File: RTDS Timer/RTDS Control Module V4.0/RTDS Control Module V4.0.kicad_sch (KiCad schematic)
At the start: 13 parts, among them J1 PH1-10-UA, K1 G6L-1P_DC5, U1 NE555D, U2 IRLML2060TRPBF

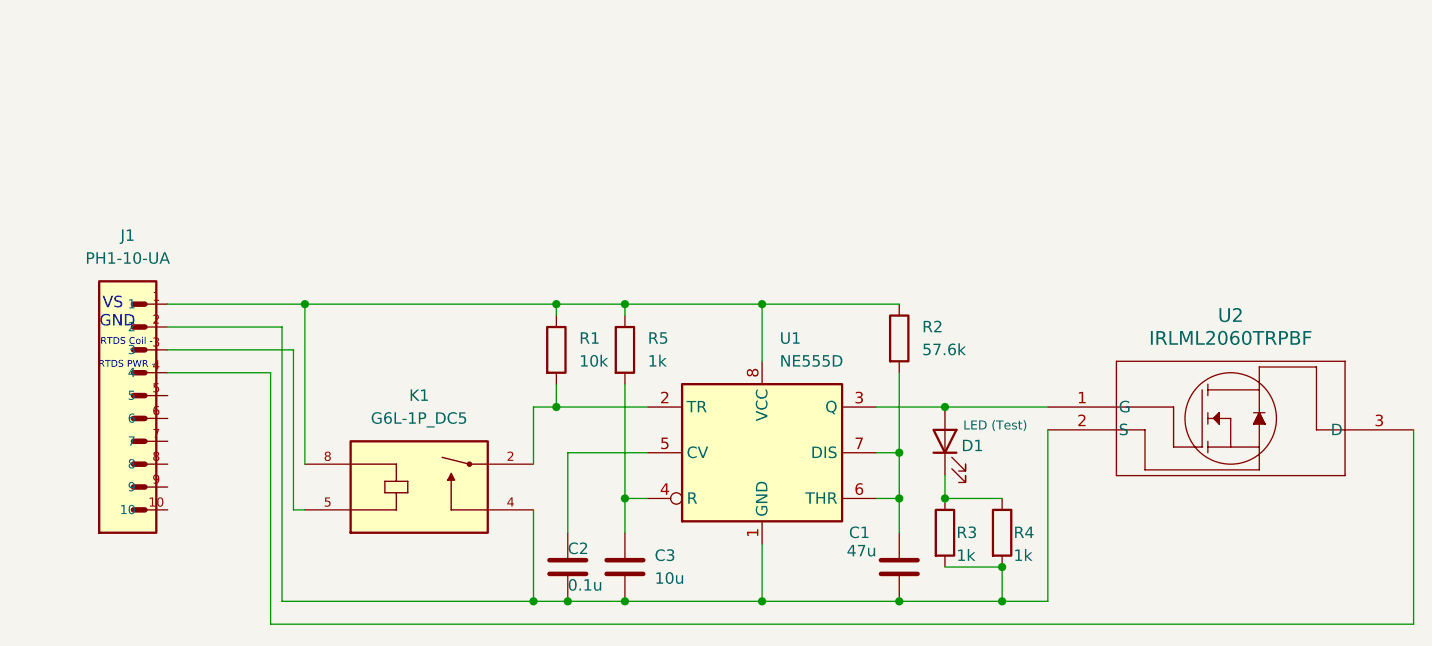
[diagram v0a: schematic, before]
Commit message: Kicad RTDS schematic changes
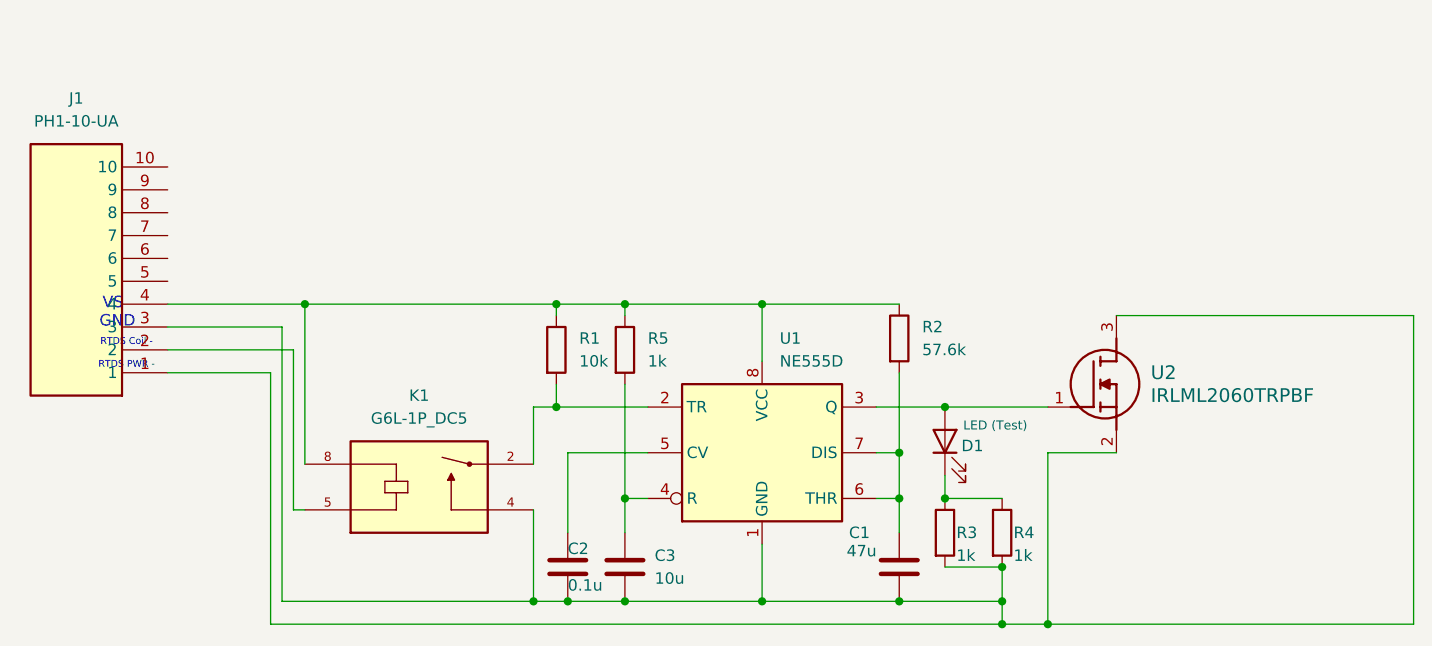
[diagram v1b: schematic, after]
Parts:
- J1: footprint 10 pin output:1X10-2.54MM-THT -> HDRV10W64P0X254_1X10_2540X249X886P; symbol 10 pin output:PH1-10-UA -> PH1-10-UA:PH1-10-UA; Arrow Part Number (none) -> PH1-10-UA; Arrow Price/Stock (none) -> null?utm_currency=USD&region=nac; Height (none) -> 8.865; Manufacturer_Name (none) -> Adam Tech; Manufacturer_Part_Number (none) -> PH1-10-UA; Mouser Part Number (none) -> 737-PH1-10-UA; Mouser Price/Stock (none) -> https://www.mouser.co.uk/ProductDetail/Adam-Tech/PH1-10-UA?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
- K1: footprint RTDS Relay:RELAY_G6L-1P_DC5 -> G6L-1P_DC5:RELAY_G6L-1P_DC5; symbol Relay:G6L-1P_DC5 -> G6L-1P_DC5:G6L-1P_DC5
- U2: footprint NMOS:SOT23_INF -> SOT95P237X112-3N; Arrow Part Number (none) -> IRLML2060TRPBF; Arrow Price/Stock (none) -> https://www.arrow.com/en/products/irlml2060trpbf/infineon-t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; Height (none) -> 1.12; Manufacturer_Name (none) -> Infineon; Manufacturer_Part_Number (none) -> IRLML2060TRPBF; Mouser Part Number (none) -> 942-IRLML2060TRPBF; Mouser Price/Stock (none) -> https://www.mouser.co.uk/ProductDetail/Infineon-Technologie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
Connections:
- net at K1.8, R1.1, R2.1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: now also J1.4; no longer J1.1
- net at C1.2, C2.2, C3.2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: now also J1.1, J1.3, U2.3 (D); no longer J1.2
- net at K1.5: now also J1.2; no longer J1.3

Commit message: Renaming stuff on boards that was wrong
RTDS schematic was totally totally wrong with the pins compared to the PCB
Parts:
- J1: symbol PH1-10-UA:PH1-10-UA -> Symbols:PH1-10-UA
- K1: symbol G6L-1P_DC5:G6L-1P_DC5 -> Symbols:G6L-1P_DC5
- U2: symbol IRLML2060TRPBF:IRLML2060TRPBF -> Symbols:IRLML2060TRPBF
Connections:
- net at K1.8, R1.1, R2.1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: now also J1.1; no longer J1.4
- net at C1.2, C2.2, C3.2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: now also J1.2, J1.4; no longer J1.1, J1.3
- net at K1.5: now also J1.3; no longer J1.2
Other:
- moved on the sheet: J1
